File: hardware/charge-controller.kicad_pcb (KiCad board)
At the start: 2 copper layers, 93.5 x 53 mm, 49 parts, among them J1 Conn_02x04_Odd_Even, J2 Conn_02x03_Odd_Even, J3 CAN_TERM, Q1 NCV8402xST, Q2 NCV8402xST, Q3 NCV8402xST, Q4 NCV8402xST, Q5 MMBT3904, Q6 MMBT3904, U1 TPS62160DGK, U2 Pico, U3 MCP2515-xST, U4 SN65HVD230

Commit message: finish inputs
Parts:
- C5: value 1u -> 100n
- R2, R4, R6, R8: value 4.7k -> 5.6k
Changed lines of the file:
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@@
   )
   (setup
-    (last_trace_width 0.8)
+    (last_trace_width 0.25)
     (user_trace_width 0.4)
     (user_trace_width 0.8)
@@
     (add_net "Net-(R13-Pad1)")
     (add_net "Net-(R14-Pad2)")
+    (add_net "Net-(U2-Pad1)")
+    (add_net "Net-(U2-Pad10)")
+    (add_net "Net-(U2-Pad11)")
+    (add_net "Net-(U2-Pad15)")
+    (add_net "Net-(U2-Pad2)")
+    (add_net "Net-(U2-Pad20)")
+    (add_net "Net-(U2-Pad30)")
+    (add_net "Net-(U2-Pad35)")
+    (add_net "Net-(U2-Pad37)")
+    (add_net "Net-(U2-Pad40)")
+    (add_net "Net-(U2-Pad41)")
+    (add_net "Net-(U2-Pad43)")
+    (add_net "Net-(U2-Pad5)")
+    (add_net "Net-(U2-Pad7)")
+    (add_net "Net-(U3-Pad11)")
+    (add_net "Net-(U3-Pad12)")
+    (add_net "Net-(U3-Pad15)")
+    (add_net "Net-(U3-Pad3)")
+    (add_net "Net-(U3-Pad4)")
+    (add_net "Net-(U3-Pad5)")
+    (add_net "Net-(U3-Pad6)")
+    (add_net "Net-(U3-Pad7)")
+    (add_net "Net-(U3-Pad8)")
+    (add_net "Net-(U4-Pad5)")
     (add_net OUT1)
     (add_net OUT12_1)
@@
       (effects (font (size 1 1) (thickness 0.15)))
     )
-    (fp_text value 4.7k (at 0 1.43 90) (layer F.Fab)
+    (fp_text value 5.6k (at 0 1.43 90) (layer F.Fab)
       (effects (font (size 1 1) (thickness 0.15)))
     )
@@
       (effects (font (size 1 1) (thickness 0.15)))
     )
-    (fp_text value 4.7k (at 0 1.43 90) (layer F.Fab)
+    (fp_text value 5.6k (at 0 1.43 90) (layer F.Fab)
       (effects (font (size 1 1) (thickness 0.15)))
     )
@@
       (effects (font (size 1 1) (thickness 0.15)))
     )
-    (fp_text value 4.7k (at 0 1.43 90) (layer F.Fab)
+    (fp_text value 5.6k (at 0 1.43 90) (layer F.Fab)
       (effects (font (size 1 1) (thickness 0.15)))
     )
@@
       (effects (font (size 1 1) (thickness 0.15)))
     )
-    (fp_text value 4.7k (at 0 1.43 90) (layer F.Fab)
+    (fp_text value 5.6k (at 0 1.43 90) (layer F.Fab)
       (effects (font (size 1 1) (thickness 0.15)))
     )
@@
       (effects (font (size 1 1) (thickness 0.15)))
     )
-    (fp_text value 1u (at 0 1.43 90) (layer F.Fab)
+    (fp_text value 100n (at 0 1.43 90) (layer F.Fab)
       (effects (font (size 1 1) (thickness 0.15)))
     )
@@
     (connect_pads yes (clearance 0))
     (min_thickness 0.254)
-    (fill (arc_segments 32) (thermal_gap 0.508) (thermal_bridge_width 0.508))
+    (fill yes (arc_segments 32) (thermal_gap 0.508) (thermal_bridge_width 0.508))
     (polygon
       (pts
@@
     (connect_pads yes (clearance 0))
     (min_thickness 0.254)
-    (fill (arc_segments 32) (thermal_gap 0.508) (thermal_bridge_width 0.508))
+    (fill yes (arc_segments 32) (thermal_gap 0.508) (thermal_bridge_width 0.508))
     (polygon
       (pts
@@
     (connect_pads yes (clearance 0))
     (min_thickness 0.254)
-    (fill (arc_segments 32) (thermal_gap 0.508) (thermal_bridge_width 0.508))
+    (fill yes (arc_segments 32) (thermal_gap 0.508) (thermal_bridge_width 0.508))
     (polygon
       (pts
@@
     (connect_pads yes (clearance 0))
     (min_thickness 0.254)
-    (fill (arc_segments 32) (thermal_gap 0.508) (thermal_bridge_width 0.508))
+    (fill yes (arc_segments 32) (thermal_gap 0.508) (thermal_bridge_width 0.508))
     (polygon
       (pts
@@
     (connect_pads yes (clearance 0.508))
     (min_thickness 0.254)
-    (fill (arc_segments 32) (thermal_gap 0.508) (thermal_bridge_width 0.508))
+    (fill yes (arc_segments 32) (thermal_gap 0.508) (thermal_bridge_width 0.508))
     (polygon
       (pts
@@
     (connect_pads yes (clearance 0))
     (min_thickness 0.254)
-    (fill (arc_segments 32) (thermal_gap 0.508) (thermal_bridge_width 0.508))
+    (fill yes (arc_segments 32) (thermal_gap 0.508) (thermal_bridge_width 0.508))
     (polygon
       (pts
@@
     (connect_pads yes (clearance 0))
     (min_thickness 0.254)
-    (fill (arc_segments 32) (thermal_gap 0.508) (thermal_bridge_width 0.508))
+    (fill yes (arc_segments 32) (thermal_gap 0.508) (thermal_bridge_width 0.508))
     (polygon
       (pts

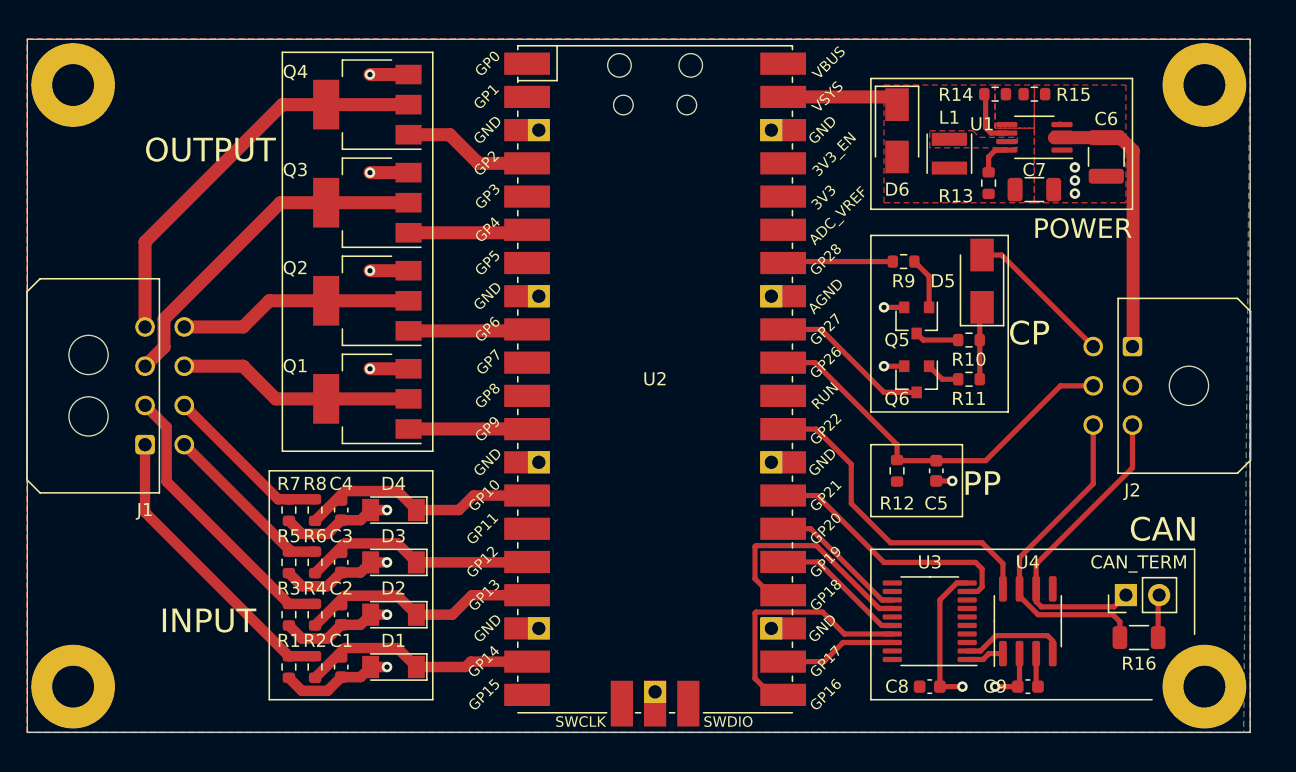
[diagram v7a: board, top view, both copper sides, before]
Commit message: hardware fix for CP line
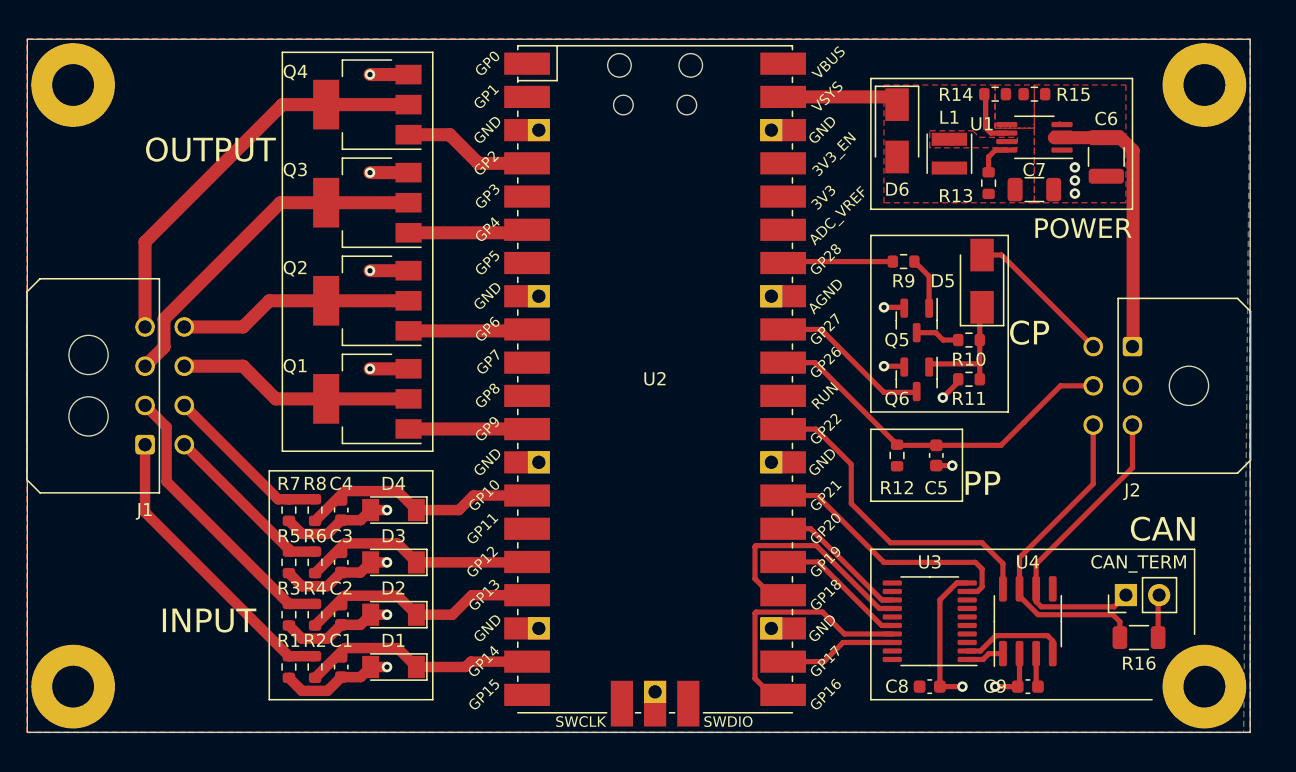
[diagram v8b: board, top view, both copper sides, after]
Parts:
- Q6: value MMBT3904 -> 2N7002
- U4: value SN65HVD230 -> SN65HVD231
- moved C5 1.17 mm to (152.0, 93.8)
- moved R12 1.17 mm to (149.0, 93.8)
- turned R11 to 0 degrees
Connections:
- Q6 pad 1: Net-(Q6-Pad1) -> Net-(D5-Pad1)
- R11 pad 1: Net-(D5-Pad1) -> GND
- R11 pad 2: Net-(Q6-Pad1) -> Net-(D5-Pad1)
- U2 pad 1: (no net) -> unconnected-(U2-Pad1)
- U2 pad 10: (no net) -> unconnected-(U2-Pad10)
- U2 pad 11: (no net) -> unconnected-(U2-Pad11)
- U2 pad 15: (no net) -> unconnected-(U2-Pad15)
- U2 pad 2: (no net) -> unconnected-(U2-Pad2)
- U2 pad 20: (no net) -> unconnected-(U2-Pad20)
- U2 pad 30: (no net) -> unconnected-(U2-Pad30)
- U2 pad 35: (no net) -> unconnected-(U2-Pad35)
- U2 pad 37: (no net) -> unconnected-(U2-Pad37)
- U2 pad 40: (no net) -> unconnected-(U2-Pad40)
- U2 pad 41: (no net) -> unconnected-(U2-Pad41)
- U2 pad 43: (no net) -> unconnected-(U2-Pad43)
- U2 pad 5: (no net) -> unconnected-(U2-Pad5)
- U2 pad 7: (no net) -> unconnected-(U2-Pad7)
- U3 pad 11: (no net) -> unconnected-(U3-Pad11)
- U3 pad 12: (no net) -> unconnected-(U3-Pad12)
- U3 pad 15: (no net) -> unconnected-(U3-Pad15)
- U3 pad 3: (no net) -> unconnected-(U3-Pad3)
- U3 pad 4: (no net) -> unconnected-(U3-Pad4)
- U3 pad 5: (no net) -> unconnected-(U3-Pad5)
- U3 pad 6: (no net) -> unconnected-(U3-Pad6)
- U3 pad 7: (no net) -> unconnected-(U3-Pad7)
- U3 pad 8: (no net) -> unconnected-(U3-Pad8)
- U4 pad 5: (no net) -> unconnected-(U4-Pad5)
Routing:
- net Net-(D5-Pad1): track 5.57 -> 9.55 mm
- net Net-(Q6-Pad1): track 2.64 -> 0.00 mm
- net GND: track 66.1 -> 68.0 mm, vias 16 -> 17
- net EVSE_PP: track 30.8 -> 29.1 mm
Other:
- net class Default removed
- net class Diff removed
- board text added: "Charge Conteoller v5"
- board text removed: "Charge Conteoller v3"
